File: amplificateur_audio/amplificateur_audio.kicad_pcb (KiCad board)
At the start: 2 copper layers, 50 parts, among them J2 Conn_01x02, J3 Conn_01x03, K1 Relay_1CT, Q1 Q_PNP_EBC, Q10 Q_PNP_BCE, Q11 BC636, Q12 Q_NPN_BCE, Q13 Q_NPN_EBC, Q2 Q_PNP_EBC, Q3 Q_PNP_EBC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

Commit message: pcb layout v2
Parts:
- added RV1: R_POT, CmpAmpliAudio:Potentiometer_Bourns_3296W_Vertical, F.Cu at (96.3, 72.9)
- added RV2: R_POT, CmpAmpliAudio:Potentiometer_Bourns_3296W_Vertical, F.Cu at (65.8, 89.4)
- C1, C3: footprint Capacitor_THT:CP_Radial_D8.0mm_P5.00mm -> CmpAmpliAudio:CP_Radial_D8.0mm_P5.00mm
- C10: value CP -> 470u; footprint Capacitor_THT:CP_Radial_D4.0mm_P1.50mm -> CmpAmpliAudio:CP_Radial_D12.5mm_P5.00mm
- C11, C2, C9: footprint Capacitor_THT:C_Rect_L7.2mm_W3.5mm_P5.00mm_FKS2_FKP2_MKS2_MKP2 -> CmpAmpliAudio:C_Rect_L7.2mm_W3.5mm_P5.00mm_FKS2_FKP2_MKS2_MKP2
- C4, C6: value CP -> 10u; footprint Capacitor_THT:CP_Radial_D4.0mm_P1.50mm -> CmpAmpliAudio:C_Rect_L7.2mm_W3.5mm_P5.00mm_FKS2_FKP2_MKS2_MKP2
- C5, C7: value C -> 100n; footprint Capacitor_THT:C_Rect_L7.2mm_W3.5mm_P5.00mm_FKS2_FKP2_MKS2_MKP2 -> CmpAmpliAudio:C_Rect_L7.2mm_W3.5mm_P5.00mm_FKS2_FKP2_MKS2_MKP2
- C8: footprint Capacitor_THT:CP_Radial_D12.5mm_P5.00mm -> CmpAmpliAudio:CP_Radial_D12.5mm_P5.00mm
- D1, D2, D3: footprint Diode_THT:D_DO-35_SOD27_P10.16mm_Horizontal -> CmpAmpliAudio:D_DO-35_SOD27_P10.16mm_Horizontal
- HS1, HS2: footprint Heatsink:Heatsink_Fischer_SK104-STC-STIC_35x13mm_2xDrill2.5mm -> CmpAmpliAudio:Heatsink_Fischer_SK104-STC-STIC_35x13mm_2xDrill2.5mm
- J2: footprint Connector_Phoenix_MSTB:PhoenixContact_MSTBVA_2,5_2-G-5,08_1x02_P5.08mm_Vertical -> CmpAmpliAudio:PhoenixContact_MSTBVA_2,5_2-G-5,08_1x02_P5.08mm_Vertical
- J3: footprint Connector_Phoenix_MSTB:PhoenixContact_MSTBVA_2,5_3-G-5,08_1x03_P5.08mm_Vertical -> CmpAmpliAudio:PhoenixContact_MSTBVA_2,5_3-G-5,08_1x03_P5.08mm_Vertical
- Q1, Q13, Q2, Q3, Q4, Q5, Q6, Q7: footprint Package_TO_SOT_THT:TO-18-3 -> CmpAmpliAudio:TO-18-3
- Q10, Q12: footprint Package_TO_SOT_THT:TO-220-3_Vertical -> CmpAmpliAudio:TO-220-3_Vertical
- Q11, Q8, Q9: footprint Package_TO_SOT_THT:TO-126-3_Vertical -> CmpAmpliAudio:TO-126-3_Vertical
- R1, R10, R13, R14, R15, R16, R17, R2, R3, R4, R5, R6, R7, R8, R9: footprint Resistor_THT:R_Axial_DIN0207_L6.3mm_D2.5mm_P10.16mm_Horizontal -> CmpAmpliAudio:R_Axial_DIN0207_L6.3mm_D2.5mm_P10.16mm_Horizontal
- R11, R12: footprint Resistor_THT:R_Axial_DIN0516_L15.5mm_D5.0mm_P20.32mm_Horizontal -> CmpAmpliAudio:R_Axial_DIN0516_L15.5mm_D5.0mm_P20.32mm_Horizontal
- moved Q8 89.4 mm to (137.2, 80.3), turned to 90 degrees
- moved R8 58.7 mm to (105.4, 105.4)
- moved R5 44.0 mm to (52.6, 128.8), turned to 90 degrees
- moved R16 37.9 mm to (113.5, 66.8)
- moved Q13 35.5 mm to (95.2, 56.6), turned to 270 degrees
- moved C8 35.1 mm to (98.6, 84.6), turned to 270 degrees
- moved Q6 34.7 mm to (73.9, 63.0)
- moved Q7 34.3 mm to (65.8, 63.0)
- moved R9 32.0 mm to (70.4, 69.1), turned to 270 degrees
- moved K1 31.9 mm to (114.3, 82.0), turned to 180 degrees
- moved C3 31.7 mm to (105.9, 51.6), turned to 90 degrees
- moved R14 30.2 mm to (100.3, 105.4), turned to 90 degrees
- moved R17 28.9 mm to (102.6, 66.8), turned to 90 degrees
- moved R7 26.0 mm to (74.9, 79.2), turned to 90 degrees
- moved R6 25.6 mm to (77.5, 102.6), turned to 90 degrees
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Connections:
- J2 pad 1: Net-(J2-Pad1) -> GND
- J2 pad 2: GND -> Net-(J2-Pad2)
- K1 pad c2: Net-(J2-Pad1) -> Net-(J2-Pad2)
- Q8 pad 3: Net-(Q6-Pad3) -> Net-(Q8-Pad3)
- R10 pad 1: GND -> Net-(R10-Pad1)
- R8 pad 2: Net-(Q6-Pad3) -> Net-(R8-Pad2)
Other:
- rule via_min_size: 0.4 -> 0.2
- board text added: "Maya Abi Ghanem - 3IMACS_D - 2020/2021 - Amplificateur Audio v2"
- board text removed: "Maya Abi Ghanem - 3IMACS_D - 2020/2021 - Amplificateur Audio v1"

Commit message: modif DRC
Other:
- net class +12V added: clearance 0.4, trace_width 1.2, via_dia 1, via_drill 0.6
- net class -12V added: clearance 0.4, trace_width 1.2, via_dia 1, via_drill 0.6
- net class Default: clearance 0.2 -> 0.3; trace_width 0.25 -> 0.7; via_dia 0.8 -> 1; via_drill 0.4 -> 0.6
- rule trace_clearance: 0.2 -> 0.3
- rule trace_min: 0.2 -> 0.6
- rule via_min_size: 0.2 -> 0.6
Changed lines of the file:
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@@
   )
   (setup
-    (last_trace_width 0.25)
-    (trace_clearance 0.2)
+    (last_trace_width 0.7)
+    (trace_clearance 0.3)
     (zone_clearance 0.508)
     (zone_45_only no)
-    (trace_min 0.2)
+    (trace_min 0.6)
     (segment_width 0.2)
     (edge_width 0.15)
-    (via_size 0.8)
-    (via_drill 0.4)
-    (via_min_size 0.2)
+    (via_size 1)
+    (via_drill 0.6)
+    (via_min_size 0.6)
     (via_min_drill 0.3)
     (uvia_size 0.3)
@@
   (net 31 "Net-(U1-PadTN)")
   (net_class Default "This is the default net class."
-    (clearance 0.2)
-    (trace_width 0.25)
-    (via_dia 0.8)
-    (via_drill 0.4)
+    (clearance 0.3)
+    (trace_width 0.7)
+    (via_dia 1)
+    (via_drill 0.6)
     (uvia_dia 0.3)
     (uvia_drill 0.1)
+    (diff_pair_gap 0.3)
+    (diff_pair_width 0.7)
     (add_net +12V)
     (add_net -12V)
@@
     (add_net "Net-(U1-PadTN)")
   )
+  (net_class +12V ""
+    (clearance 0.4)
+    (trace_width 1.2)
+    (via_dia 1)
+    (via_drill 0.6)
+    (uvia_dia 0.3)
+    (uvia_drill 0.1)
+    (diff_pair_gap 0.4)
+    (diff_pair_width 1.2)
+  )
+  (net_class -12V ""
+    (clearance 0.4)
+    (trace_width 1.2)
+    (via_dia 1)
+    (via_drill 0.6)
+    (uvia_dia 0.3)
+    (uvia_drill 0.1)
+    (diff_pair_gap 0.4)
+    (diff_pair_width 1.2)
+  )
   (module CmpAmpliAudio:CP_Radial_D8.0mm_P5.00mm (layer F.Cu)

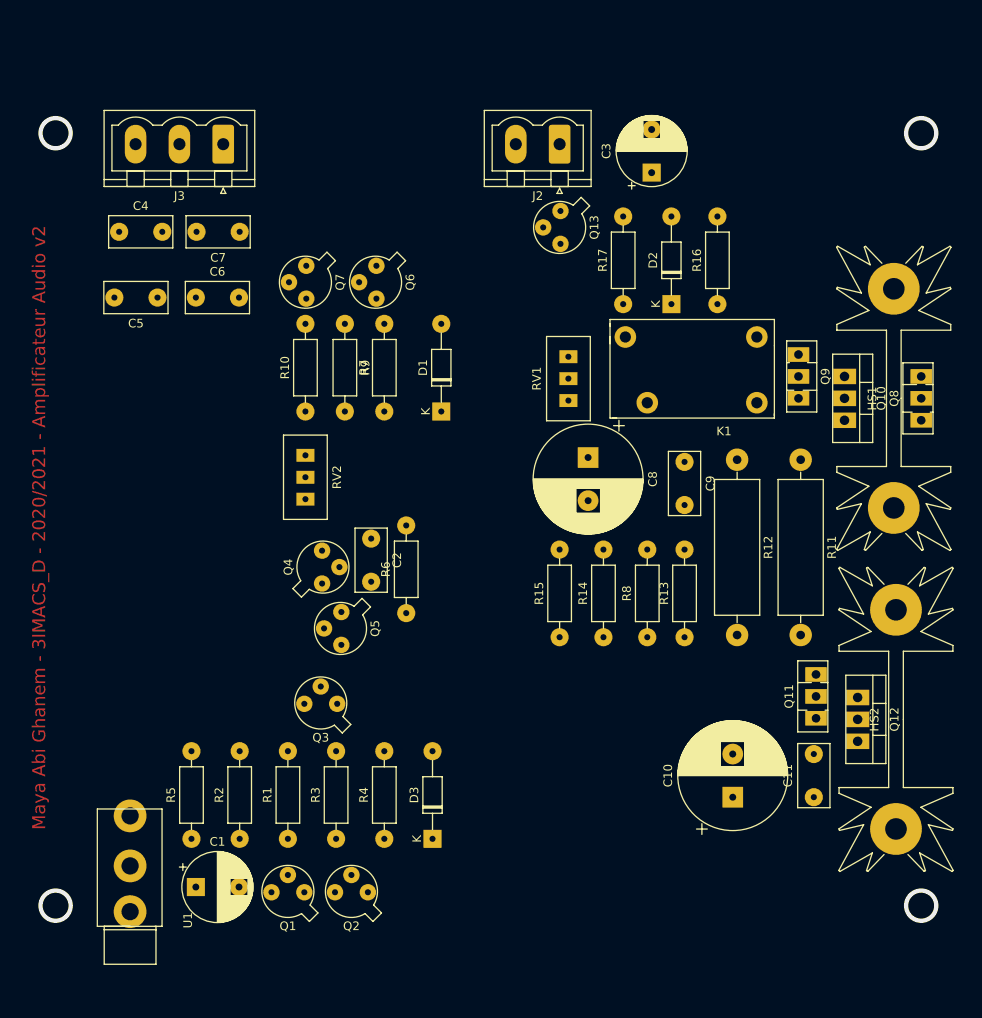
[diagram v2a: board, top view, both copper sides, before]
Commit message: v3: regroupement des composants de puissances , correction footprint relais + c4 + c6
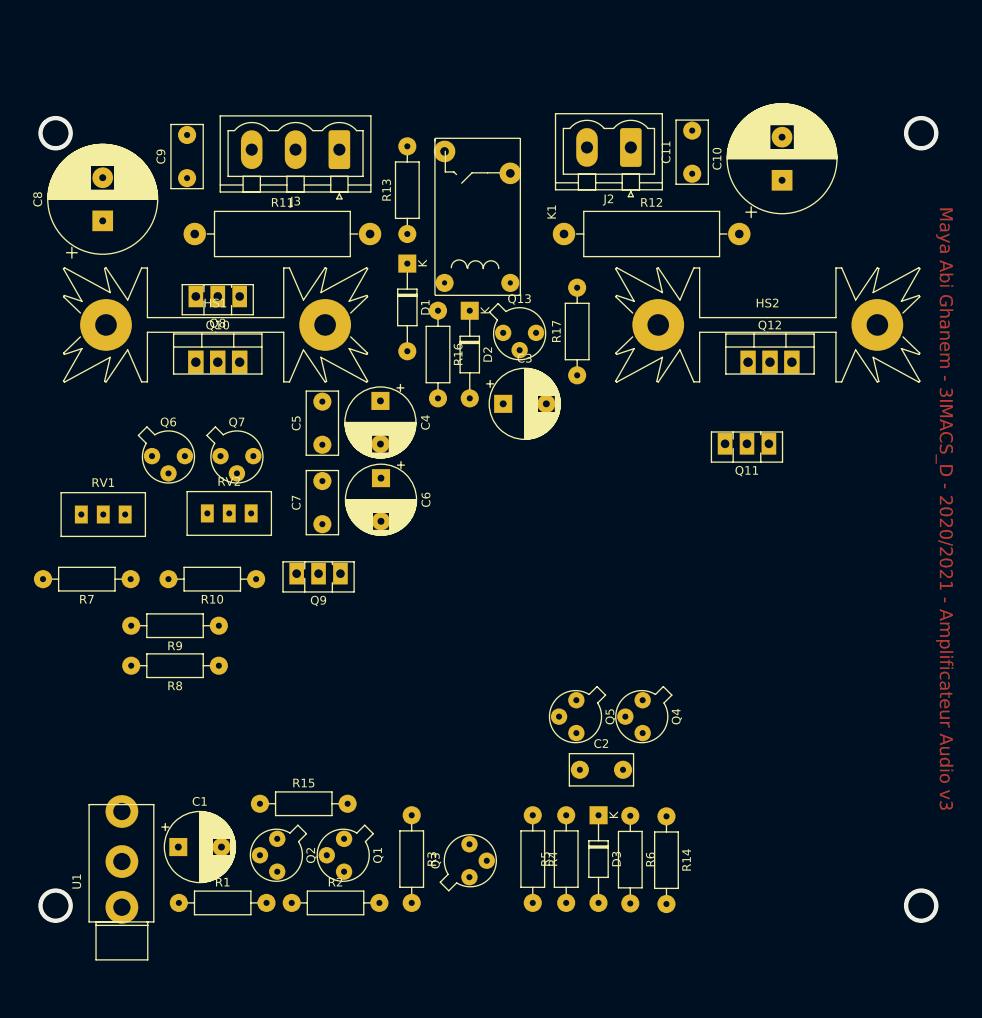
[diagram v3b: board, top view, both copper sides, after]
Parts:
- C4, C6: footprint CmpAmpliAudio:C_Rect_L7.2mm_W3.5mm_P5.00mm_FKS2_FKP2_MKS2_MKP2 -> CmpAmpliAudio:CP_Radial_D8.0mm_P5.00mm
- K1: footprint be_elec_footprint:Relais_112LMH2 -> CmpAmpliAudioTR:Relais_112LMH2
- moved Q8 80.3 mm to (58.2, 65.9), turned to 180 degrees
- moved HS1 79.1 mm to (55.4, 69.2), turned to 0 degrees
- moved Q10 75.2 mm to (53.1, 73.5), turned to 0 degrees
- moved R11 74.9 mm to (53.0, 58.7), turned to 0 degrees
- moved C11 73.6 mm to (110.6, 51.7)
- moved C10 71.7 mm to (121.0, 52.5)
- moved C9 66.4 mm to (52.1, 52.2), turned to 90 degrees
- moved C8 62.6 mm to (42.3, 57.1), turned to 90 degrees
- moved Q9 58.8 mm to (69.8, 98.0), turned to 180 degrees
- moved R13 56.7 mm to (77.6, 58.7)
- moved RV1 54.5 mm to (44.9, 91.2), turned to 0 degrees
- moved R8 49.8 mm to (55.8, 108.7), turned to 180 degrees
- moved HS2 48.1 mm to (119.4, 69.2), turned to 0 degrees
- moved R5 44.1 mm to (96.0, 136.2)
- moved Q12 40.9 mm to (117.1, 73.5), turned to 0 degrees
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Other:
- board text added: "Maya Abi Ghanem - 3IMACS_D - 2020/2021 - Amplificateur Audio v3"
- board text removed: "Maya Abi Ghanem - 3IMACS_D - 2020/2021 - Amplificateur Audio v2"

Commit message: ajout pistes
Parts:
- moved D3 56.4 mm to (49.9, 99.6)
- moved R9 55.0 mm to (109.6, 93.0), turned to 90 degrees
- moved R7 54.7 mm to (97.9, 82.8), turned to 270 degrees
- moved Q7 54.4 mm to (109.5, 97.4), turned to 270 degrees
- moved Q6 52.0 mm to (98.3, 99.9), turned to 90 degrees
- moved R15 51.5 mm to (111.0, 114.7), turned to 90 degrees
- moved R5 46.8 mm to (49.9, 128.0)
- moved R14 44.5 mm to (82.4, 89.5)
- moved Q2 42.1 mm to (103.4, 119.9)
- moved R10 40.9 mm to (97.7, 114.7), turned to 90 degrees
- moved R6 39.9 mm to (125.9, 93.1), turned to 90 degrees
- moved R4 37.6 mm to (65.3, 99.7)
- moved RV2 34.9 mm to (90.3, 107.6), turned to 90 degrees
- moved R8 34.1 mm to (36.3, 80.6), turned to 0 degrees
- moved Q5 32.6 mm to (127.4, 101.2)
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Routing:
- net +12V: track 0.00 -> 240.5 mm
- net -12V: track 0.00 -> 229.3 mm, vias 0 -> 6
- net Net-(C2-Pad1): track 0.00 -> 199.5 mm, vias 0 -> 2
- net Net-(K1-Padc1): track 0.00 -> 79.7 mm
- net Net-(Q10-Pad1): track 0.00 -> 71.1 mm
- net Net-(Q10-Pad2): track 0.00 -> 57.1 mm, vias 0 -> 4
- net Net-(Q6-Pad3): track 0.00 -> 54.8 mm
- net Net-(Q6-Pad1): track 0.00 -> 47.9 mm
- net Net-(C2-Pad2): track 0.00 -> 43.8 mm
- net Net-(Q11-Pad1): track 0.00 -> 38.6 mm
- net Net-(Q1-Pad1): track 0.00 -> 38.3 mm
- net Net-(Q11-Pad2): track 0.00 -> 33.1 mm
- net Net-(C1-Pad1): track 0.00 -> 30.2 mm
- net Net-(Q4-Pad1): track 0.00 -> 28.3 mm
- net Net-(D1-Pad2): track 0.00 -> 28.3 mm
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
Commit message: routage + ajout de plan de masse
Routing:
- net Net-(Q6-Pad3): track 54.8 -> 128.8 mm
- net -12V: track 229.3 -> 270.0 mm, vias 6 -> 7
- net +12V: track 240.5 -> 258.8 mm
- added copper zone on B.Cu, net GND
- added copper zone on F.Cu, net GND
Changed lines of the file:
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@@
     (thickness 1.6)
     (drawings 10)
-    (tracks 304)
+    (tracks 328)
     (zones 0)
     (modules 52)
@@
   (segment (start 65.663324 94.554779) (end 66.04 94.178103) (width 0.8) (layer B.Cu) (net 6))
   (segment (start 66.04 94.178103) (end 76.073 84.145103) (width 0.8) (layer B.Cu) (net 6))
+  (segment (start 112.2045 48.491424) (end 112.2045 47.0065) (width 2) (layer F.Cu) (net 6))
+  (segment (start 103.967499 56.728425) (end 112.2045 48.491424) (width 2) (layer F.Cu) (net 6))
+  (segment (start 103.967499 73.754503) (end 103.967499 56.728425) (width 2) (layer F.Cu) (net 6))
+  (segment (start 99.490002 78.232) (end 99.490002 78.232) (width 2) (layer F.Cu) (net 6))
+  (segment (start 99.490002 78.232) (end 103.967499 73.754503) (width 2) (layer F.Cu) (net 6))
+  (via (at 99.490002 78.232) (size 2) (drill 1) (layers F.Cu B.Cu) (net 6))
+  (segment (start 99.490002 78.232) (end 95.297 78.232) (width 2) (layer B.Cu) (net 6))
   (segment (start 54.991 52.197) (end 52.07 52.197) (width 2) (layer B.Cu) (net 8))
   (segment (start 59.563 48.895) (end 58.293 48.895) (width 2) (layer B.Cu) (net 8))
@@
   (segment (start 60.706 73.152) (end 59.055 74.803) (width 2) (layer B.Cu) (net 8))
   (segment (start 79.1845 62.4205) (end 76.1345 62.4205) (width 2) (layer B.Cu) (net 8))
-  (segment (start 76.010999 62.544001) (end 67.630999 62.544001) (width 2) (layer B.Cu) (net 8))
   (segment (start 67.630999 62.544001) (end 60.706 69.469) (width 2) (layer B.Cu) (net 8))
   (segment (start 80.990499 85.125501) (end 80.137 85.979) (width 0.8) (layer B.Cu) (net 8))
@@
   (segment (start 82.7405 67.8815) (end 80.990499 69.631501) (width 0.8) (layer B.Cu) (net 8))
   (segment (start 60.706 69.469) (end 60.706 73.152) (width 2) (layer B.Cu) (net 8))
+  (segment (start 68.962001 62.544001) (end 69.723 62.544001) (width 2) (layer B.Cu) (net 8))
+  (segment (start 59.563 48.895) (end 59.563 53.145) (width 2) (layer B.Cu) (net 8))
+  (segment (start 76.010999 62.544001) (end 69.723 62.544001) (width 2) (layer B.Cu) (net 8))
+  (segment (start 59.563 53.145) (end 68.962001 62.544001) (width 2) (layer B.Cu) (net 8))
+  (segment (start 69.723 62.544001) (end 67.630999 62.544001) (width 2) (layer B.Cu) (net 8))
   (segment (start 92.607424 64.6605) (end 92.624924 64.643) (width 2) (layer B.Cu) (net 9))
   (segment (start 91.1225 64.6605) (end 92.607424 64.6605) (width 2) (layer B.Cu) (net 9))
@@
   (segment (start 57.43 80.645) (end 62.094399 85.309399) (width 0.8) (layer B.Cu) (net 22))
   (segment (start 55.88 80.645) (end 57.43 80.645) (width 0.8) (layer B.Cu) (net 22))
+  (segment (start 55.626 65.282998) (end 55.626 67.183) (width 2) (layer F.Cu) (net 22))
+  (segment (start 54.976001 64.632999) (end 55.626 65.282998) (width 2) (layer F.Cu) (net 22))
+  (segment (start 51.195999 64.632999) (end 54.976001 64.632999) (width 2) (layer F.Cu) (net 22))
+  (segment (start 49.863695 53.800695) (end 49.863695 63.300695) (width 2) (layer F.Cu) (net 22))
+  (segment (start 41.155001 51.046999) (end 47.109999 51.046999) (width 2) (layer F.Cu) (net 22))
+  (segment (start 55.88 79.044998) (end 55.130001 78.294999) (width 2) (layer F.Cu) (net 22))
+  (segment (start 55.88 80.645) (end 55.88 79.044998) (width 2) (layer F.Cu) (net 22))
+  (segment (start 36.322 70.499002) (end 36.322 55.88) (width 2) (layer F.Cu) (net 22))
+  (segment (start 47.109999 51.046999) (end 49.863695 53.800695) (width 2) (layer F.Cu) (net 22))
+  (segment (start 55.130001 78.294999) (end 44.117997 78.294999) (width 2) (layer F.Cu) (net 22))
+  (segment (start 49.863695 63.300695) (end 51.195999 64.632999) (width 2) (layer F.Cu) (net 22))
+  (segment (start 44.117997 78.294999) (end 36.322 70.499002) (width 2) (layer F.Cu) (net 22))
+  (segment (start 36.322 55.88) (end 41.155001 51.046999) (width 2) (layer F.Cu) (net 22))
   (segment (start 109.601 96.747) (end 109.574 96.774) (width 0.8) (layer B.Cu) (net 23))
   (segment (start 109.601 92.964) (end 109.601 96.747) (width 0.8) (layer B.Cu) (net 23))
@@
   (segment (start 97.663 114.681) (end 90.779 114.681) (width 0.8) (layer B.Cu) (net 30))
   (segment (start 90.297 110.109) (end 90.297 112.649) (width 0.8) (layer B.Cu) (net 30))
+  (zone (net 7) (net_name GND) (layer B.Cu) (hatch edge 0.508)
+    (connect_pads (clearance 0.508))
+    (min_thickness 0.254)
+    (fill yes (arc_segments 16) (thermal_gap 0.508) (thermal_bridge_width 0.508))
+    (polygon
+      (pts
+        (xy 32.385 43.18) (xy 142.24 43.18) (xy 142.24 139.7) (xy 32.385 139.7)
+      )
+    )
+  )
+  (zone (net 7) (net_name GND) (layer F.Cu) (hatch edge 0.508)
+    (connect_pads (clearance 0.508))
+    (min_thickness 0.254)
+    (fill yes (arc_segments 16) (thermal_gap 0.508) (thermal_bridge_width 0.508))
+    (polygon
+      (pts
+        (xy 32.512 43.307) (xy 141.986 43.18) (xy 142.24 139.7) (xy 32.385 139.7) (xy 32.385 43.307)
+        (xy 32.385 43.18)
+      )
+    )
+  )
 )

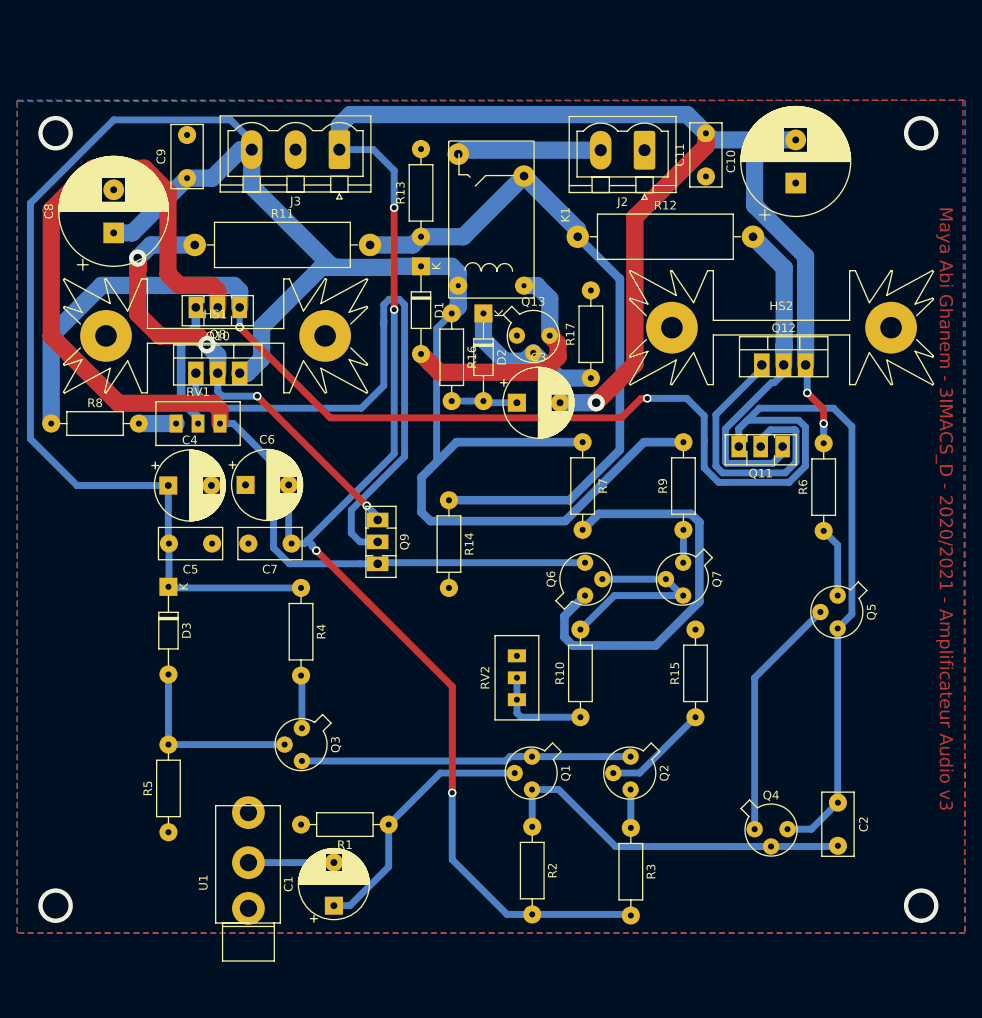
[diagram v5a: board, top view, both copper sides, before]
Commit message: pcb layout with added diodes
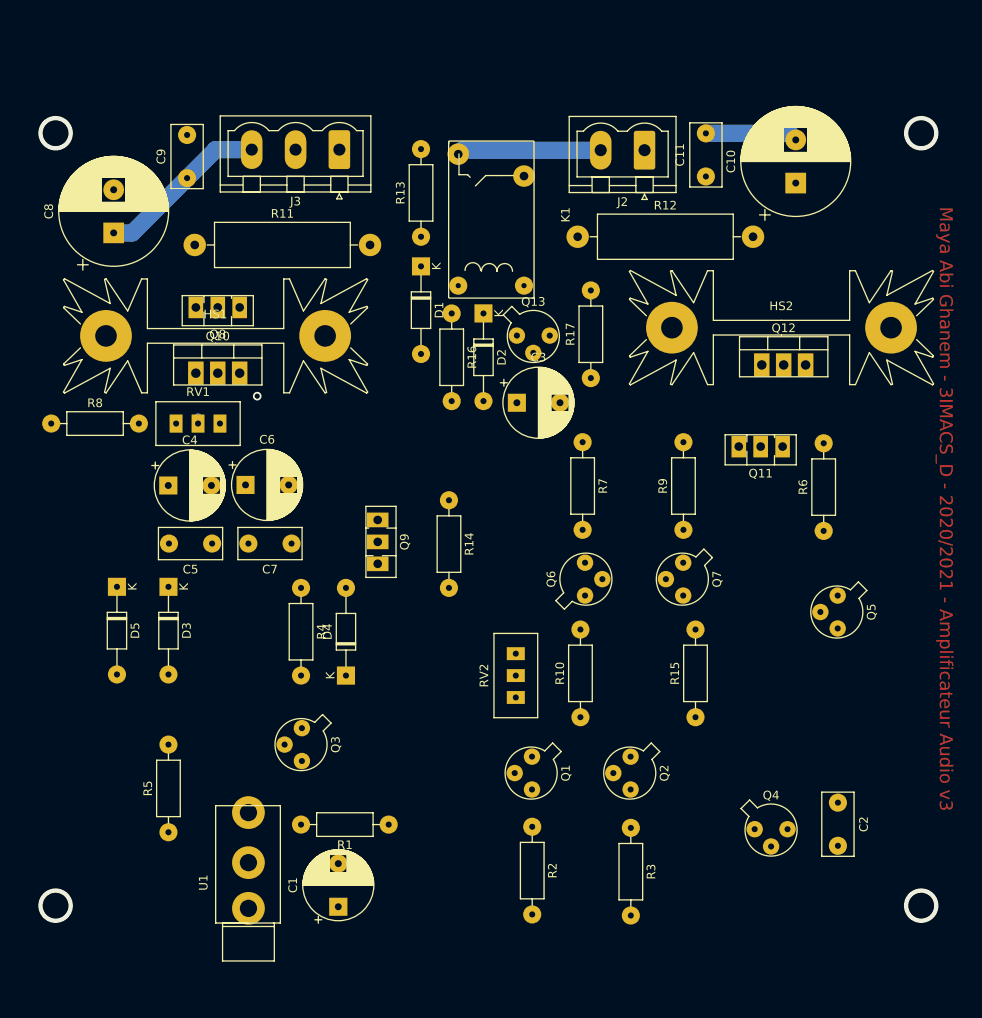
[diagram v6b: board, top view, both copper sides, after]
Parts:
- added D4: D, CmpAmpliAudio:D_DO-35_SOD27_P10.16mm_Horizontal, F.Cu at (70.5, 109.9)
- added D5: D, CmpAmpliAudio:D_DO-35_SOD27_P10.16mm_Horizontal, F.Cu at (43.9, 99.6)
- moved C1 0.52 mm to (69.6, 136.7)
- moved RV2 0.28 mm to (90.2, 107.3)
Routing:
- net -12V: track 270.0 -> 12.4 mm, vias 7 -> 0
- net +12V: track 258.8 -> 20.0 mm
- net Net-(C2-Pad1): track 199.5 -> 0.04 mm, vias 2 -> 0
- net Net-(Q6-Pad3): track 128.8 -> 0.18 mm
- net Net-(K1-Padc1): track 79.7 -> 0.00 mm
- net Net-(Q10-Pad1): track 71.1 -> 0.00 mm
- net Net-(Q10-Pad2): track 57.1 -> 0.76 mm, vias 4 -> 1
- net Net-(Q6-Pad1): track 47.9 -> 0.00 mm
- net Net-(C2-Pad2): track 43.8 -> 0.11 mm
- net Net-(Q1-Pad1): track 38.3 -> 0.00 mm
- net Net-(Q11-Pad1): track 38.6 -> 0.97 mm
- net Net-(Q11-Pad2): track 33.1 -> 1.27 mm
- net Net-(C1-Pad1): track 30.2 -> 0.00 mm
- net Net-(Q4-Pad1): track 28.3 -> 0.00 mm
- net Net-(D1-Pad2): track 28.3 -> 0.00 mm
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- removed copper zone on B.Cu, net GND
- removed copper zone on F.Cu, net GND
